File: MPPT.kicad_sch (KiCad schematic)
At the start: 49 parts, among them IC2 LM5109BQNGTRQ1, IC7 ISO6520REUR, J1 MX150_02x08_RightAngle, J3 Conn_01x01_Pin, J4 Conn_01x01_Pin, J5 Conn_01x01_Pin, J6 Conn_01x01_Pin, J7 Conn_01x01_Pin, J8 Conn_01x01_Pin, Q1 IPB95R450PFD7ATMA1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

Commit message: Minor changes to connectors and amplifiers
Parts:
- removed J1: MX150_02x08_RightAngle, UTSVT_Connectors:CONN_SD-75900-001_2X08_MOL, symbol utsvt_connectors:MX150_02x08_RightAngle
- removed J7, J8: Conn_01x01_Pin, 973582101:973582101, symbol Connector:Conn_01x01_Pin
- added J2: MX150_02x04_RightAngle, UTSVT_Connectors:CONN_SD-75900-001_2X04_MOL, symbol utsvt_connectors:MX150_02x04_RightAngle
- added R14, R15: 0, symbol Device:R
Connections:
- net +24V: now also J2.1 (+24V), J2.4 (PWR_OUT*)
- net CAN_H: now also J2.2 (CANH_IN), J2.6 (CANH_OUT)
- net CAN_L: now also J2.3 (CANL_IN), J2.7 (CANL_OUT)
- net GND: now also J2.5 (GND), J2.8 (GND_OUT*)
- net H_Gate: now also R14.1; no longer IC2.7 (HO)
- net L_Gate: now also R15.1; no longer IC2.5 (LO)
- new net: IC2.7 (HO), R14.2
- new net: IC2.5 (LO), R15.2
- no-connect marks 24 -> 16
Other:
- note added: "Anderson Connectors?"
- note removed: "Banana Cables"
- note removed: "Battery is load 12v_In and Array are supplies"
- moved on the sheet: J3, J4, J5, J6

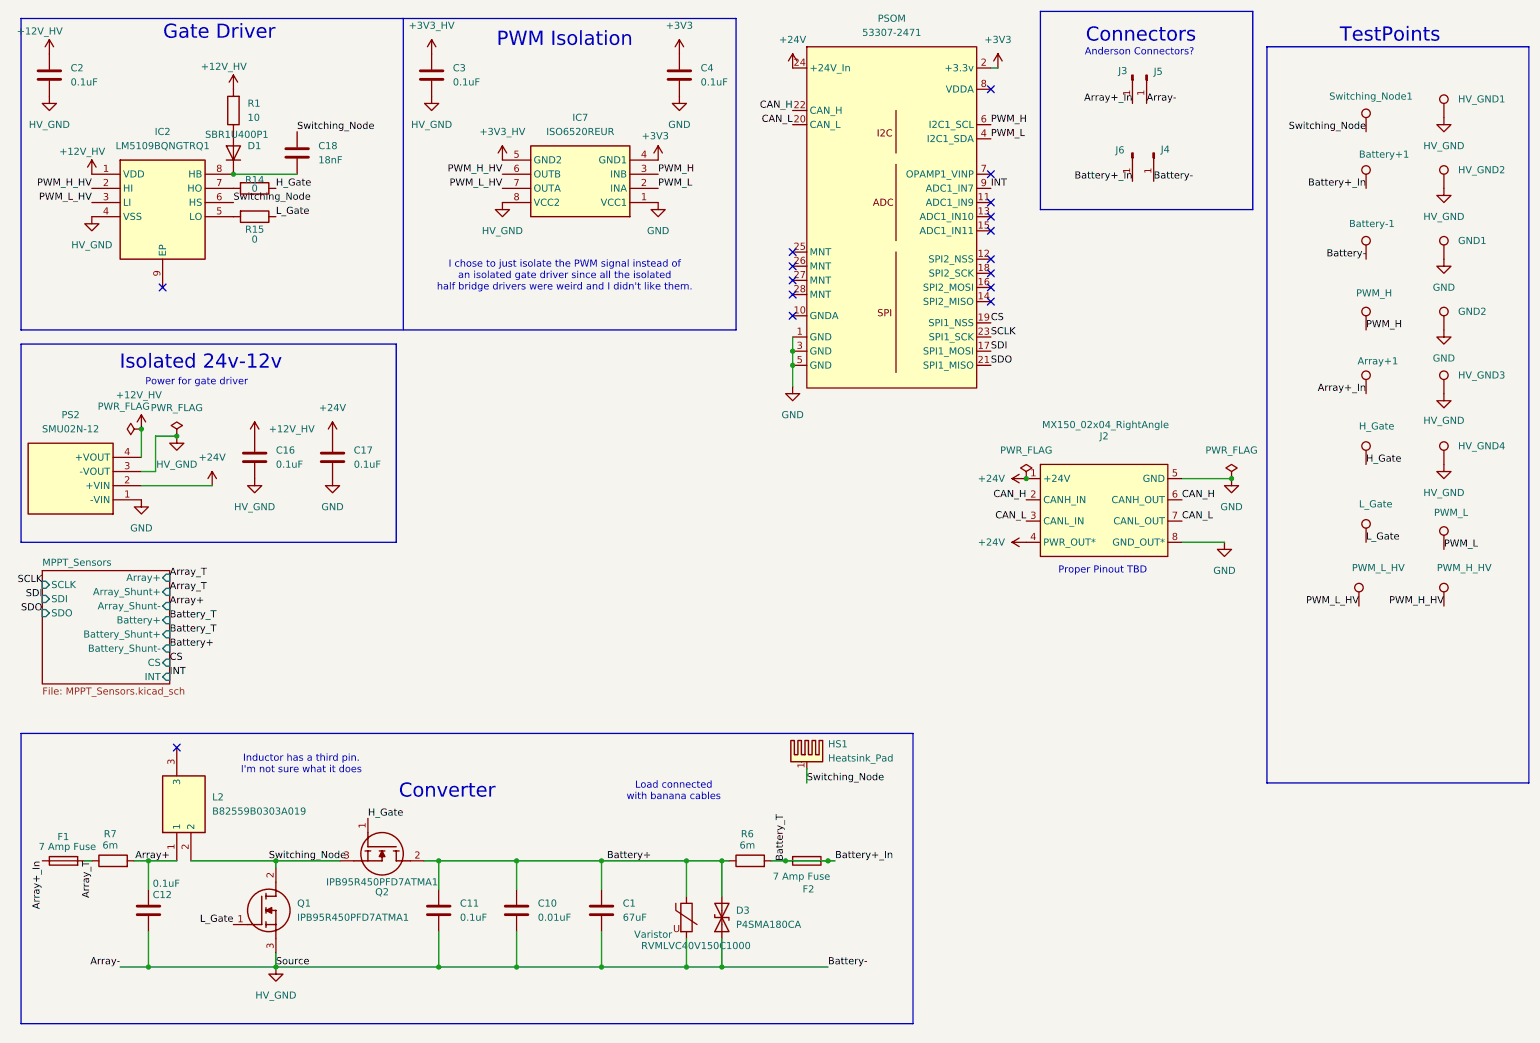
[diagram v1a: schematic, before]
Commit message: Fixed PSOM pinout, added 24v-3.3v iso supply, moved current sensing to low side
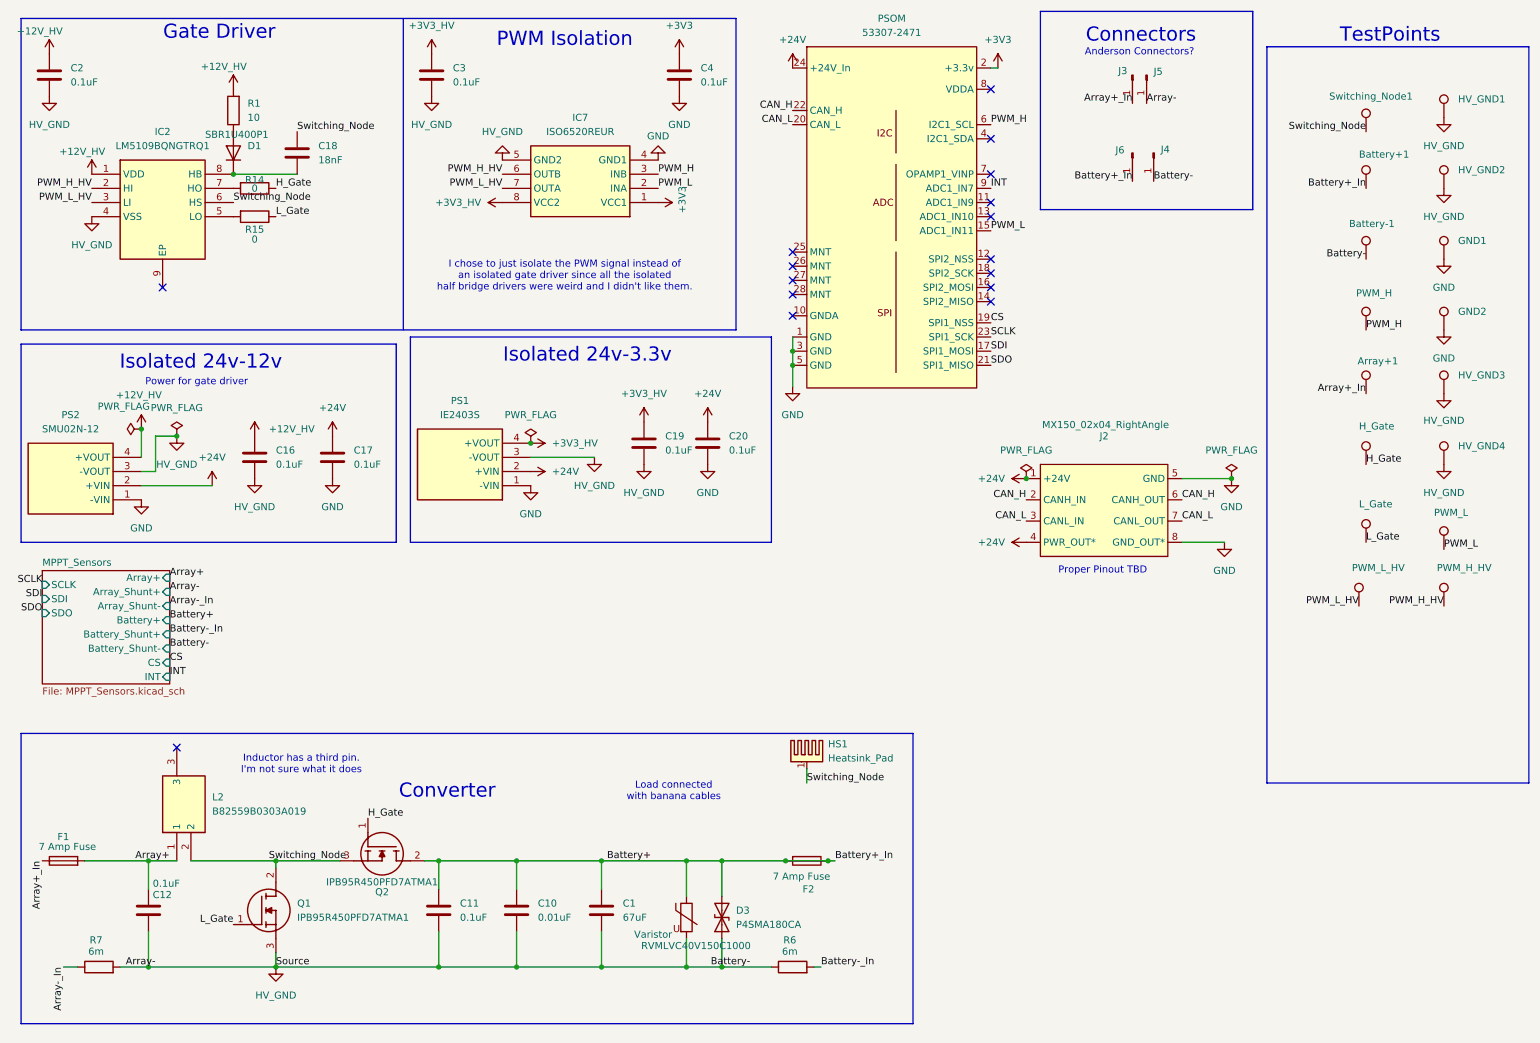
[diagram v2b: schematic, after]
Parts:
- added C19, C20: 0.1uF, Capacitor_SMD:C_0805_2012Metric, symbol Device:C
- added PS1: IE2403S, IE2424S, symbol MPPT_Symbols:IE2403S
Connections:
- net +24V: now also C20.1, PS1.2 (+VIN)
- net +3V3: now also IC7.1 (VCC1); no longer IC7.4 (GND1)
- net +3V3_HV: now also IC7.8 (VCC2), C19.1, PS1.4 (+VOUT); no longer IC7.5 (GND2)
- net Array+: now also F1.2; no longer R7.2
- net Battery+: now also Battery+1.1, F2.1, F2.2, J6.1 (Pin_1); no longer R6.1
- net GND: now also IC7.4 (GND1), C20.2, PS1.1 (-VIN); no longer IC7.1 (VCC1)
- net HV_GND: now also IC7.5 (GND2), R6.1, R7.2, C19.2, PS1.3 (-VOUT); no longer IC7.8 (VCC2)
- net PWM_L: now also PSOM.15 (ADC1_IN11); no longer PSOM.4 (I2C1_SDA)
- net Array_T renamed Array-_In
- net Array-_In: no longer F1.2
- removed net Battery+_In: Battery+1.1, F2.1, F2.2, J6.1 (Pin_1), R6.2
- new net Battery-_In: R6.2
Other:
- note added: "Isolated 24v-3.3v"
- moved on the sheet: R6, R7
